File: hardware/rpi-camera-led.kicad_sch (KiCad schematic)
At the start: 20 parts, among them J1 FFC 15P 1.0mm (to Raspberry P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, J2 FFC 15P 1.0mm (to camera), J3 Qwiic (JST SH 1.0mm), J4 SWD program header 2.54mm, Q1 AO3400A, Q2 Phototransistor, U1 CH32V003A4M6

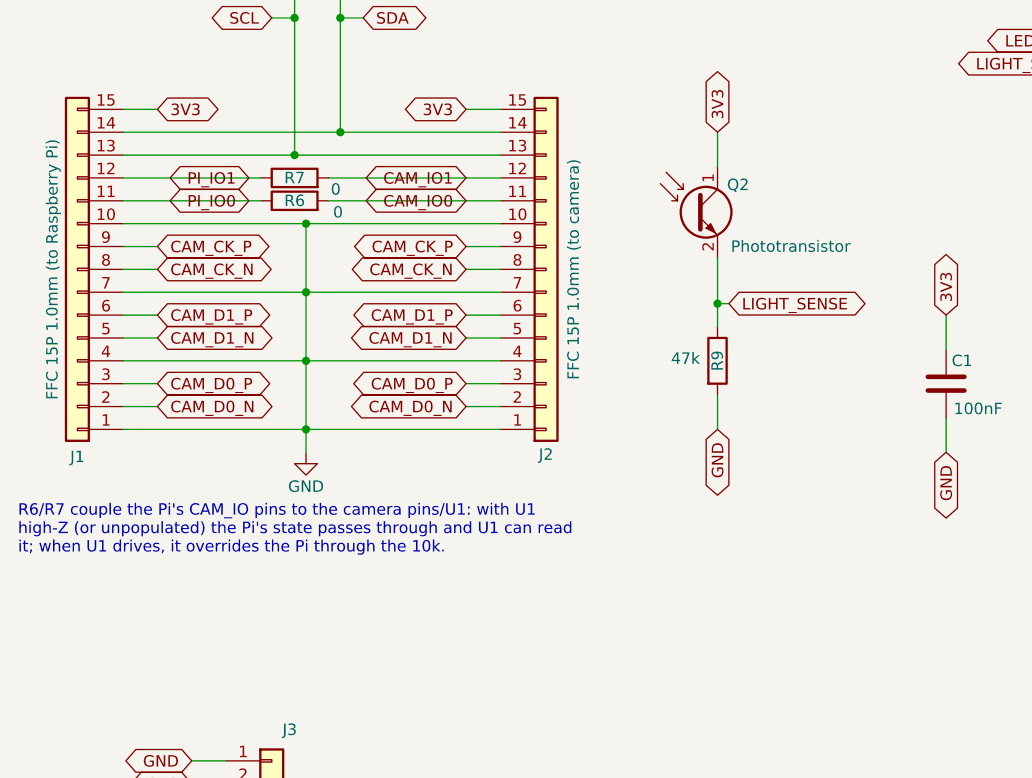
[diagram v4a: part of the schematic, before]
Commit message: Mark R6/R7 do-not-populate
The 0R links are a build option, not part of the default build: leaving
them off is what puts U1 in the middle of each GPIO channel, watching
the Pi on PD6/PD7 and driving the camera on PA1/PA2.  Fitting one ties
the Pi's pin straight to the camera, which is what you want when U1 is
unpopulated and the board is just a pass-through.

Rewrite the on-sheet note to match: it still described 10k couplers and
an override current that no longer exists.  With 0R there is nothing to
limit contention, so the note now says not to fit them while U1 drives.
Also drop the note clear of J1's reference designator, which it had
grown into.

check_schematic.py stays red on PI_IO0/CAM_IO0, unchanged by this
commit and still waiting on the pin 11 label question.

Co-Authored-By: Claude Opus 5 (1M context) <noreply@anthropic.com>
Claude-Session: https://claude.ai/code/session_01E6VQHygrbAGSqdngQQsBdx
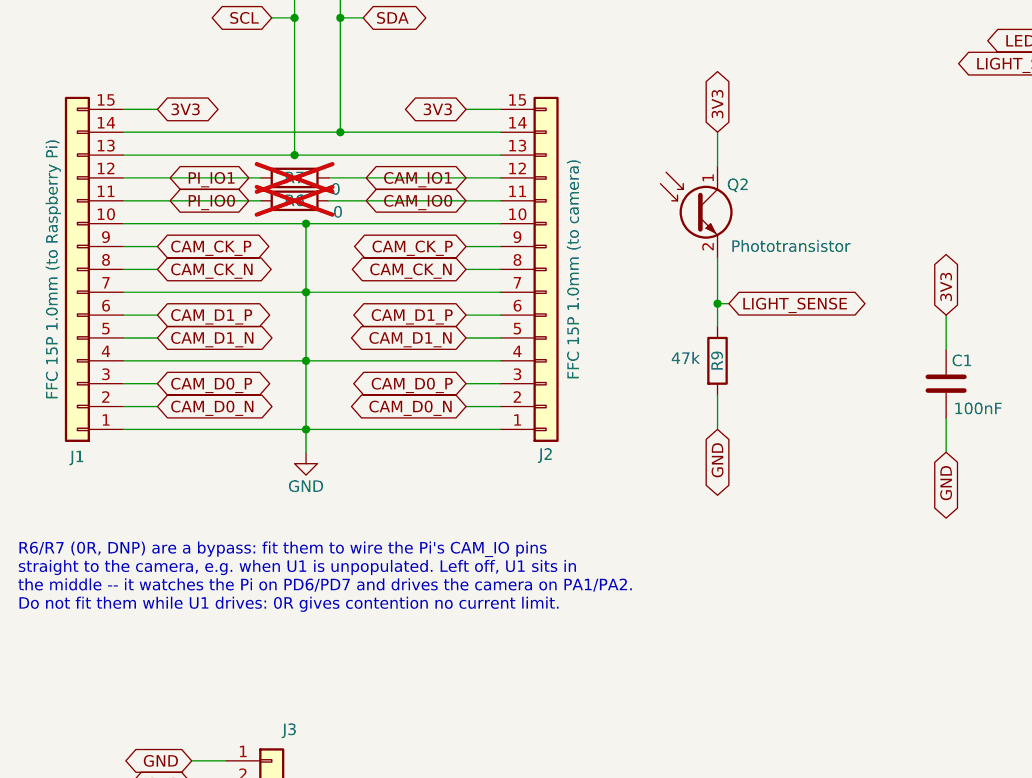
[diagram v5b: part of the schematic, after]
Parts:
- R6, R7: now not fitted
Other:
- note added: "R6/R7 (0R, DNP) are a bypass: fit them to wire the Pi's CAM_IO pins straight to the camera, e.g. when U1 is unpopulated. Left off, U1 sits in the middle -- it watches the Pi on PD6/PD7 and drives the camera on PA1/PA2. Do not fit them while U1 drives: 0R gives contention no current limit."
- note removed: "R6/R7 couple the Pi's CAM_IO pins to the camera pins/U1: with U1 high-Z (or unpopulated) the Pi's state passes through and U1 can read it; when U1 drives, it overrides the Pi through the 10k."
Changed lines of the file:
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@@
 		)
 	)
-	(text "R6/R7 couple the Pi's CAM_IO pins to the camera pins/U1: with U1\nhigh-Z (or unpopulated) the Pi's state passes through and U1 can read\nit; when U1 drives, it overrides the Pi through the 10k."
+	(text "R6/R7 (0R, DNP) are a bypass: fit them to wire the Pi's CAM_IO pins\nstraight to the camera, e.g. when U1 is unpopulated. Left off, U1 sits in\nthe middle -- it watches the Pi on PD6/PD7 and drives the camera on PA1/PA2.\nDo not fit them while U1 drives: 0R gives contention no current limit."
 		(exclude_from_sim no)
-		(at 16.256 114.3 0)
+		(at 16.256 120.65 0)
 		(effects
 			(font
@@
 		(in_bom yes)
 		(on_board yes)
-		(dnp no)
+		(dnp yes)
 		(property "Reference" "R7"
 			(at 46.99 72.39 90)
@@
 		(in_bom yes)
 		(on_board yes)
-		(dnp no)
+		(dnp yes)
 		(property "Reference" "R6"
 			(at 46.99 74.93 90)

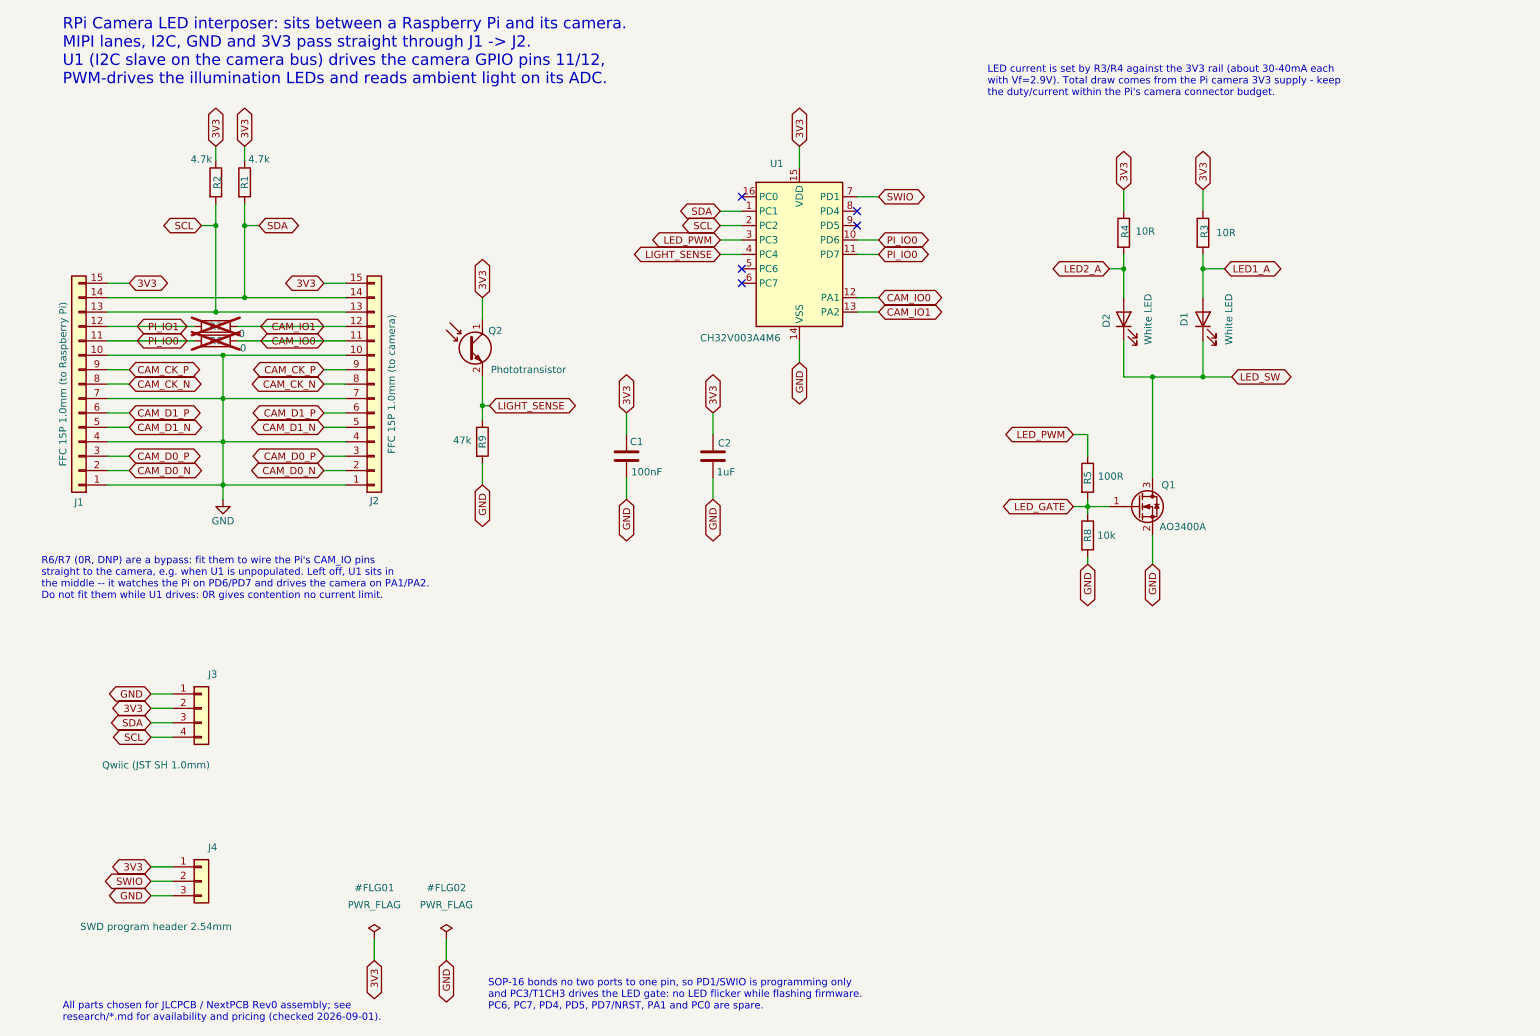
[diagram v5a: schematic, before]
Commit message: Sense the Pi's IO1 on PD5, and leave PD7 alone
Pin 11 carried a second PI_IO0 label, so PD6 and PD7 sat on one net
while PI_IO1 reached no U1 pin at all.  Rather than relabel pin 11,
move the channel-1 sense to PD5 (pin 9) and no-connect pin 11.

PD5 is the better pin on every count.  PD7 is NRST until the RST_MODE
option byte in flash says otherwise, so a Pi GPIO wired to it would
reset the MCU on any part that has not been provisioned yet -- a board
that misbehaves until firmware has run once is a bad failure mode for
something assembled in volume.  PD5 has no such second life, sits next
to PD6 so both sense pins are adjacent on port D, and mirrors the drive
pair on PA1/PA2.

    9  PD5  PI_IO1      12  PA1  CAM_IO0
    10 PD6  PI_IO0      13  PA2  CAM_IO1

check_schematic.py is green again: expected nets now describe U1
straddling each channel, PD5 moves out of the unused list and PD7 into
it with the reason recorded, and the two on-sheet notes that still said
PD6/PD7 are corrected.

Co-Authored-By: Claude Opus 5 (1M context) <noreply@anthropic.com>
Claude-Session: https://claude.ai/code/session_01E6VQHygrbAGSqdngQQsBdx
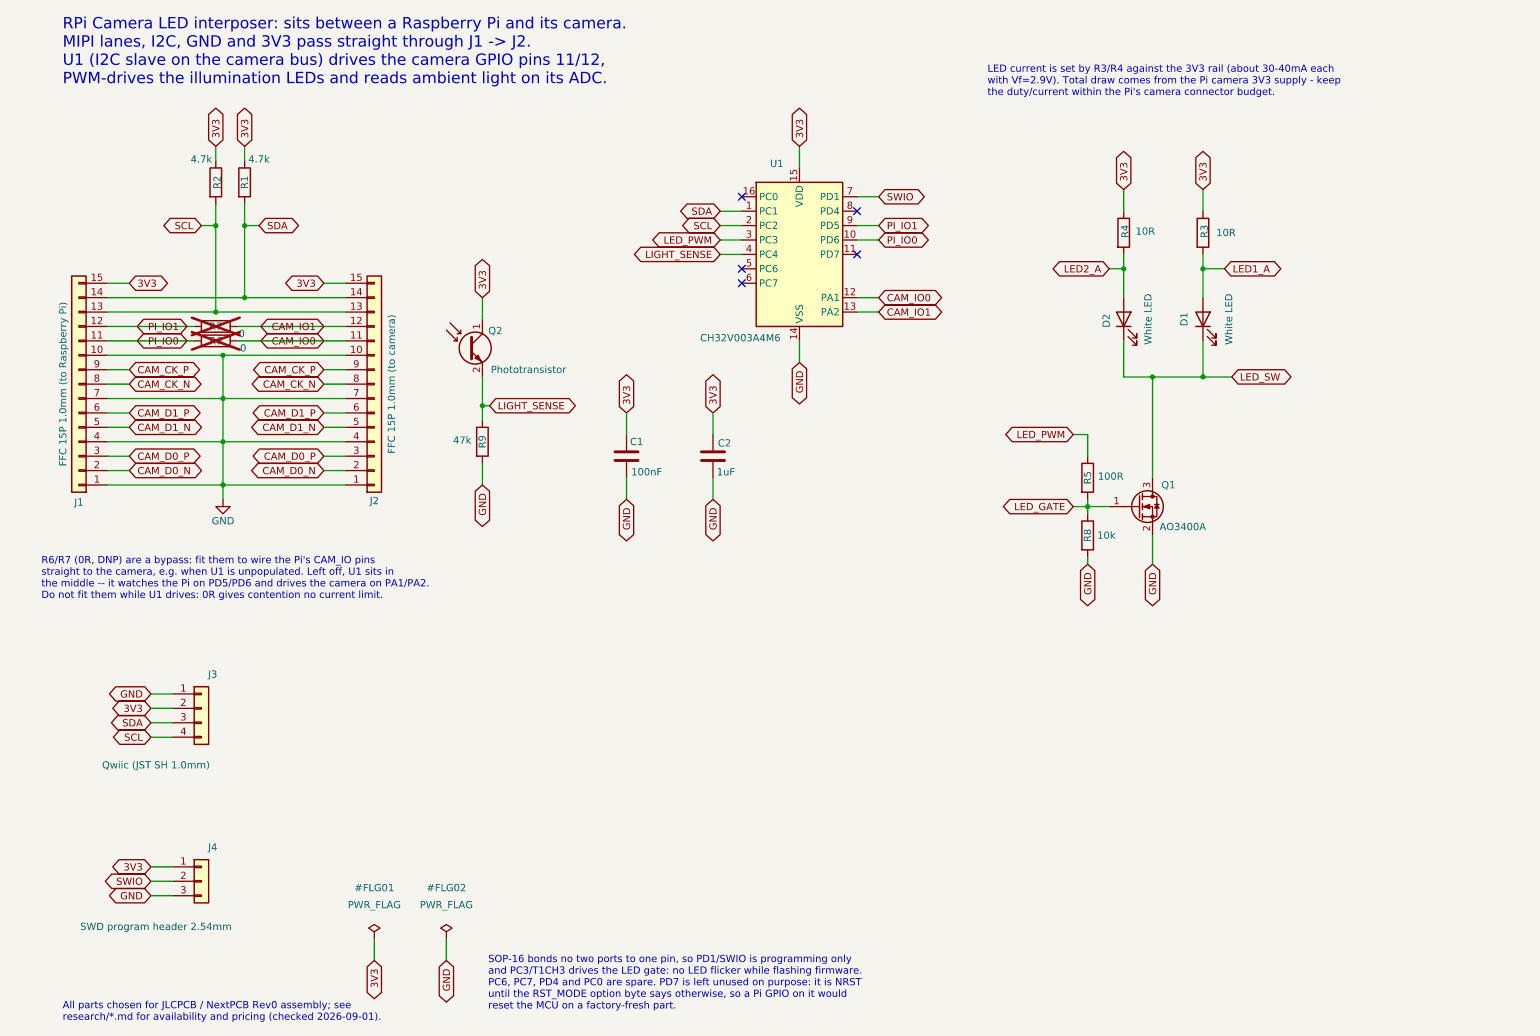
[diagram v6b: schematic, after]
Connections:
- net PI_IO0: no longer U1.11 (PD7)
- net PI_IO1: now also U1.9 (PD5)
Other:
- note added: "R6/R7 (0R, DNP) are a bypass: fit them to wire the Pi's CAM_IO pins straight to the camera, e.g. when U1 is unpopulated. Left off, U1 sits in the middle -- it watches the Pi on PD5/PD6 and drives the camera on PA1/PA2. Do not fit them while U1 drives: 0R gives contention no current limit."
- note added: "SOP-16 bonds no two ports to one pin, so PD1/SWIO is programming only and PC3/T1CH3 drives the LED gate: no LED flicker while flashing firmware. PC6, PC7, PD4 and PC0 are spare. PD7 is left unused on purpose: it is NRST until the RST_MODE option byte says otherwise, so a Pi GPIO on it would reset the MCU on a factory-fresh part."
- note removed: "R6/R7 (0R, DNP) are a bypass: fit them to wire the Pi's CAM_IO pins straight to the camera, e.g. when U1 is unpopulated. Left off, U1 sits in the middle -- it watches the Pi on PD6/PD7 and drives the camera on PA1/PA2. Do not fit them while U1 drives: 0R gives contention no current limit."
- note removed: "SOP-16 bonds no two ports to one pin, so PD1/SWIO is programming only and PC3/T1CH3 drives the LED gate: no LED flicker while flashing firmware. PC6, PC7, PD4, PD5, PD7/NRST, PA1 and PC0 are spare."
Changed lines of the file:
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@@
 		)
 	)
-	(text "R6/R7 (0R, DNP) are a bypass: fit them to wire the Pi's CAM_IO pins\nstraight to the camera, e.g. when U1 is unpopulated. Left off, U1 sits in\nthe middle -- it watches the Pi on PD6/PD7 and drives the camera on PA1/PA2.\nDo not fit them while U1 drives: 0R gives contention no current limit."
+	(text "R6/R7 (0R, DNP) are a bypass: fit them to wire the Pi's CAM_IO pins\nstraight to the camera, e.g. when U1 is unpopulated. Left off, U1 sits in\nthe middle -- it watches the Pi on PD5/PD6 and drives the camera on PA1/PA2.\nDo not fit them while U1 drives: 0R gives contention no current limit."
 		(exclude_from_sim no)
 		(at 16.256 120.65 0)
@@
 		)
 	)
-	(text "SOP-16 bonds no two ports to one pin, so PD1/SWIO is programming only\nand PC3/T1CH3 drives the LED gate: no LED flicker while flashing firmware.\nPC6, PC7, PD4, PD5, PD7/NRST, PA1 and PC0 are spare."
+	(text "SOP-16 bonds no two ports to one pin, so PD1/SWIO is programming only\nand PC3/T1CH3 drives the LED gate: no LED flicker while flashing firmware.\nPC6, PC7, PD4 and PC0 are spare. PD7 is left unused on purpose: it is NRST\nuntil the RST_MODE option byte says otherwise, so a Pi GPIO on it would\nreset the MCU on a factory-fresh part."
 		(exclude_from_sim no)
 		(at 95 193 0)
@@
 	)
 	(no_connect
-		(at 160.02 54.61)
-	)
-	(no_connect
 		(at 160.02 52.07)
 	)
@@
 	(wire
 		(pts
-			(xy 160.02 59.69) (xy 163.83 59.69)
-		)
-		(stroke
-			(width 0)
-			(type default)
-		)
-	)
-	(wire
-		(pts
 			(xy 39.37 139.7) (xy 35.56 139.7)
 		)
@@
 		)
 	)
-	(global_label "PI_IO0"
-		(shape bidirectional)
-		(at 163.83 59.69 0)
-		(fields_autoplaced yes)
-		(effects
-			(font
-				(size 1.27 1.27)
-			)
-			(justify left)
-		)
-		(property "Intersheetrefs" "${INTERSHEET_REFS}"
-			(at 173.9137 59.69 0)
-			(effects
-				(font
-					(size 1.27 1.27)
-				)
-				(justify left)
-				(hide yes)
-			)
-		)
-	)
 	(global_label "SCL"
 		(shape bidirectional)
@@
 	)
 	(embedded_fonts no)
+	(wire
+		(pts
+			(xy 160.02 54.61) (xy 163.83 54.61)
+		)
+		(stroke
+			(width 0)
+			(type default)
+		)
+	)
+	(global_label "PI_IO1"
+		(shape bidirectional)
+		(at 163.83 54.61 0)
+		(fields_autoplaced yes)
+		(effects
+			(font
+				(size 1.27 1.27)
+			)
+			(justify left)
+		)
+		(property "Intersheetrefs" "${INTERSHEET_REFS}"
+			(at 173.9137 54.61 0)
+			(effects
+				(font
+					(size 1.27 1.27)
+				)
+				(justify left)
+				(hide yes)
+			)
+		)
+	)
+	(no_connect
+		(at 160.02 59.69)
+	)
 )

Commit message: Make J2 a top-contact FFC so J1->J2 runs straight
J1 and J2 were the same bottom-contact part.  Two connectors whose
cables leave opposite edges of the board are 180 degrees apart, so pad
1 of one faces pad 15 of the other and all fifteen pass-through nets
have to cross the bus to reach their pin.

Switch J2 to the top-contact sibling, AFA07-S15ECA-00.  Contacting the
other face of the cable mirrors its conductor-to-pad order, which
cancels the rotation: pin N now faces pin N and the whole bus routes
straight across on one layer.  Per the JUSHUO series drawing the two
parts share one recommended land pattern (same 1.00 pitch, 0.60 pad
width, same 3.65/2.60/3.00/1.80/4.57 dimensions, Circuit 1 at the same
end); the part number decodes as AFA07-S <ckts> <plating> E|F * A-00
with E = Upper and F = Lower contact, so only the contact face differs.
Both are stocked by both assemblers -- ECA is C262742 at $0.1055/100
with 12,866 in stock, about a cent over the FCA.

KiCad ships only the FCA footprints, so add a project library holding a
copy renamed and re-described for the ECA part rather than leave J2
pointing at a footprint named for the wrong variant.

The catch, recorded on the sheet: the camera-side cable now goes in
contacts up, flipped relative to the Pi side.  That wants an
opposite-side (type D) FFC on that segment, or a fold in a standard
same-side one.  J1 and J2 now name their contact type in the value and
MPN fields so the mismatch reads as deliberate.

Co-Authored-By: Claude Opus 5 (1M context) <noreply@anthropic.com>
Claude-Session: https://claude.ai/code/session_01E6VQHygrbAGSqdngQQsBdx
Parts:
- J1: value FFC 15P 1.0mm (to Raspberry Pi) -> FFC 15P 1.0mm bottom contact (to Raspberry Pi); MPN JUSHUO AFA07-S15FCA-00 / Amphenol SFW15R-1STE1LF -> JUSHUO AFA07-S15FCA-00 (bottom contact, LCSC C262721)
- J2: value FFC 15P 1.0mm (to camera) -> FFC 15P 1.0mm top contact (to camera); footprint Connector_FFC-FPC:JUSHUO_AFA07-S15FCA-00_1x15-1MP_P1.0mm_Horizontal -> rpi-camera-led:JUSHUO_AFA07-S15ECA-00_1x15-1MP_P1.0mm_Horizontal; MPN JUSHUO AFA07-S15FCA-00 / Amphenol SFW15R-1STE1LF -> JUSHUO AFA07-S15ECA-00 (top contact, LCSC C262742)
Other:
- note added: "J1 and J2 are deliberately different parts: J1 bottom contact, J2 top contact. Top contact mirrors J2's cable-to-pad order, which cancels the 180 deg rotation between two connectors whose cables leave opposite edges -- so every J1->J2 net runs straight across on one layer instead of crossing the whole bus. Cost: the camera-side cable goes in contacts up, i.e. flipped from the Pi side. Use an oppo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"
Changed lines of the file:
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@@
 			)
 		)
-		(property "Value" "FFC 15P 1.0mm (to camera)"
+		(property "Value" "FFC 15P 1.0mm top contact (to camera)"
 			(at 77.978 82.55 90)
 			(effects
@@
 			)
 		)
-		(property "Footprint" "Connector_FFC-FPC:JUSHUO_AFA07-S15FCA-00_1x15-1MP_P1.0mm_Horizontal"
+		(property "Footprint" "rpi-camera-led:JUSHUO_AFA07-S15ECA-00_1x15-1MP_P1.0mm_Horizontal"
 			(at 74.93 82.55 0)
 			(effects
@@
 			)
 		)
-		(property "MPN" "JUSHUO AFA07-S15FCA-00 / Amphenol SFW15R-1STE1LF"
+		(property "MPN" "JUSHUO AFA07-S15ECA-00 (top contact, LCSC C262742)"
 			(at 74.93 82.55 0)
 			(effects
@@
 			)
 		)
-		(property "Value" "FFC 15P 1.0mm (to Raspberry Pi)"
+		(property "Value" "FFC 15P 1.0mm bottom contact (to Raspberry Pi)"
 			(at 20.066 82.55 90)
 			(effects
@@
 			)
 		)
-		(property "MPN" "JUSHUO AFA07-S15FCA-00 / Amphenol SFW15R-1STE1LF"
+		(property "MPN" "JUSHUO AFA07-S15FCA-00 (bottom contact, LCSC C262721)"
 			(at 22.86 82.55 0)
 			(effects
@@
 		(at 160.02 59.69)
 	)
+	(text "J1 and J2 are deliberately different parts: J1 bottom contact, J2 top contact.\nTop contact mirrors J2's cable-to-pad order, which cancels the 180 deg rotation\nbetween two connectors whose cables leave opposite edges -- so every J1->J2 net\nruns straight across on one layer instead of crossing the whole bus.\nCost: the camera-side cable goes in contacts up, i.e. flipped from the Pi side.\nUse an opposite-side (type D) FFC there, or fold a standard same-side one."
+		(exclude_from_sim no)
+		(at 181.61 149.86 0)
+		(effects
+			(font
+				(size 1.27 1.27)
+			)
+			(justify left bottom)
+		)
+	)
 )
